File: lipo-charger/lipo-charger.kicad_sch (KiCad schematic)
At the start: 8 parts, among them J1 USB_B_Micro, U1 MCP73831-2-OT

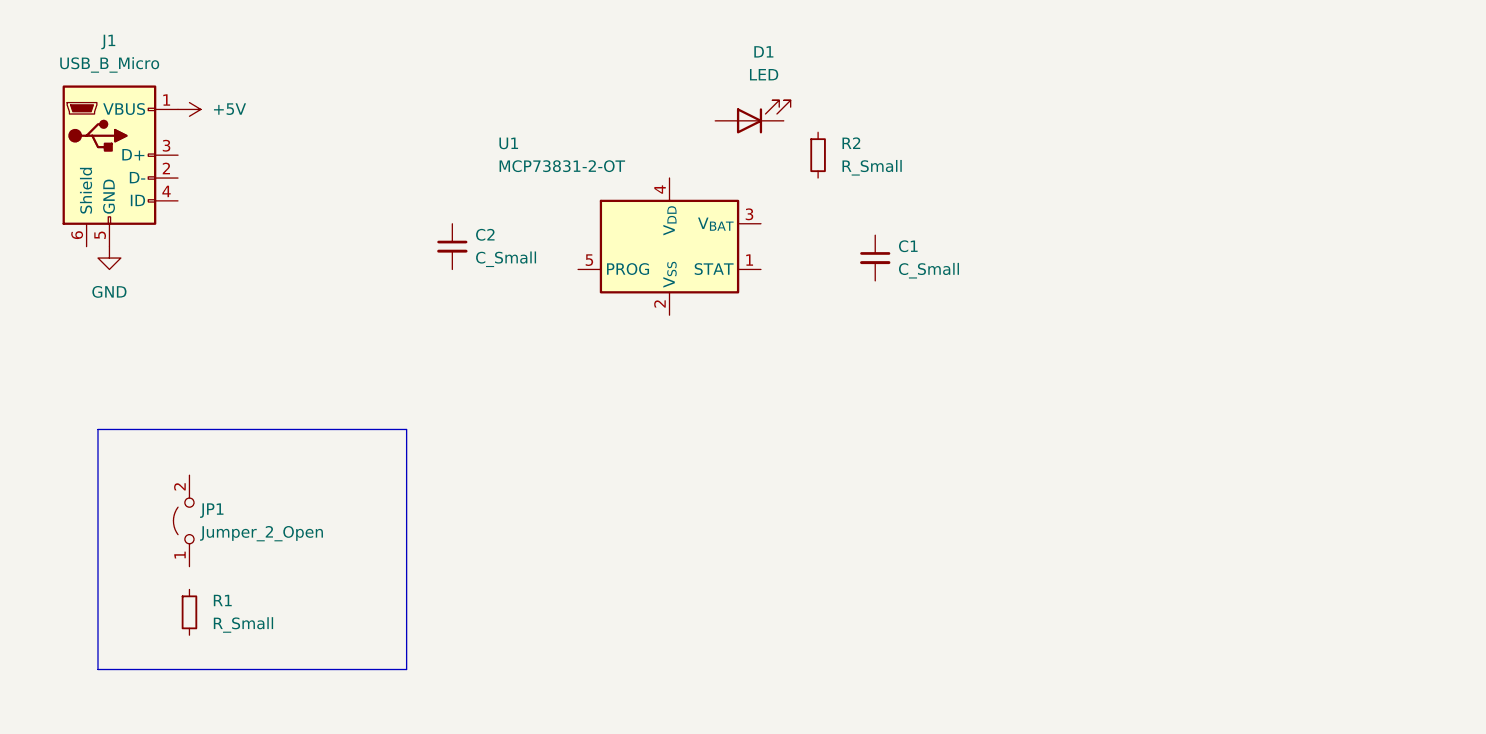
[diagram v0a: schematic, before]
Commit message: add prog resistor
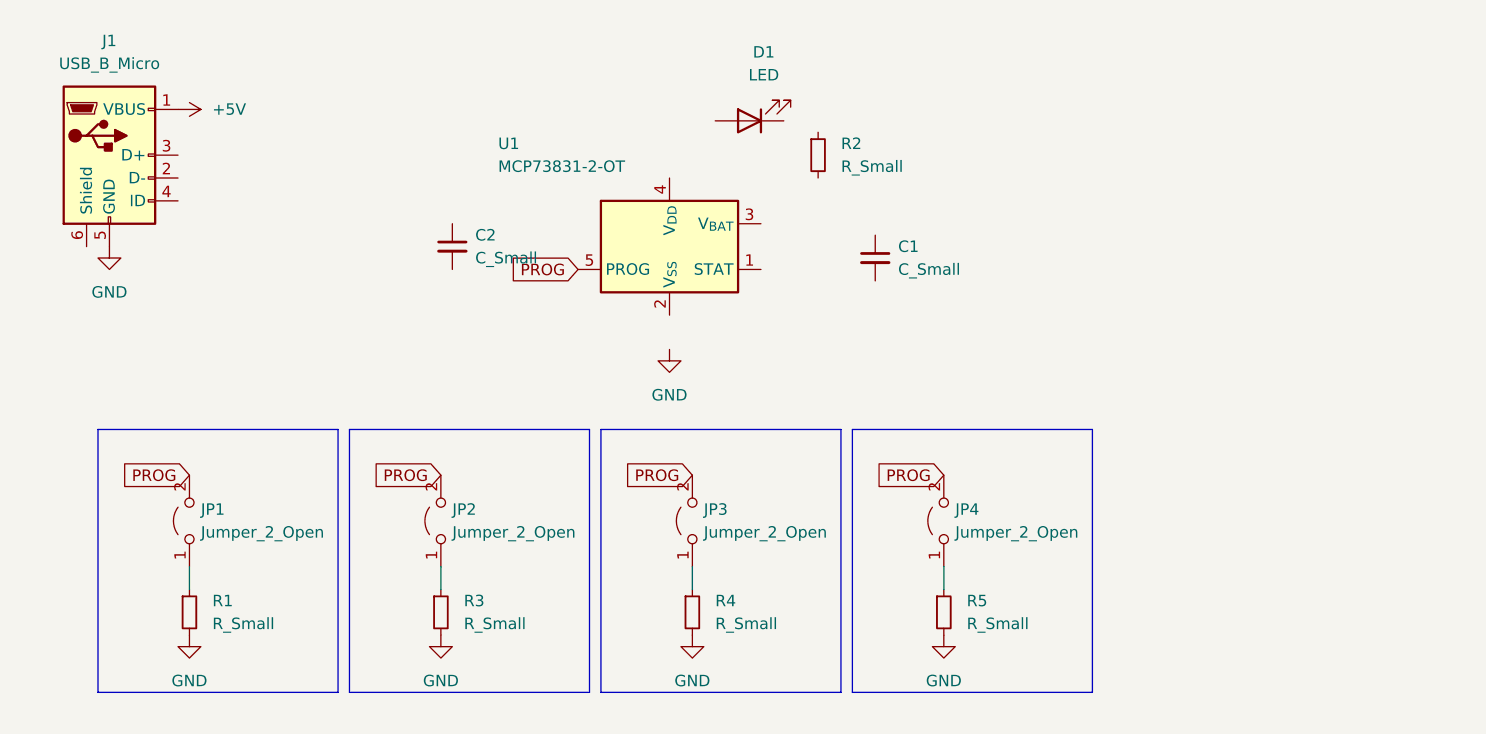
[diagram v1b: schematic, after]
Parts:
- added JP2, JP3, JP4: Jumper_2_Open, symbol Jumper:Jumper_2_Open
- added R3, R4, R5: R_Small, symbol Device:R_Small
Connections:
- net GND: now also R1.2, R3.2, R4.2, R5.2
- net at JP1.1 (A): now also R1.1
- net PROG: now reaches JP1.2 (B)
- net PROG: now also U1.5 (PROG), JP2.2 (B), JP3.2 (B), JP4.2 (B)
- new net: JP4.1 (A), R5.1
- new net: JP3.1 (A), R4.1
- new net: JP2.1 (A), R3.1

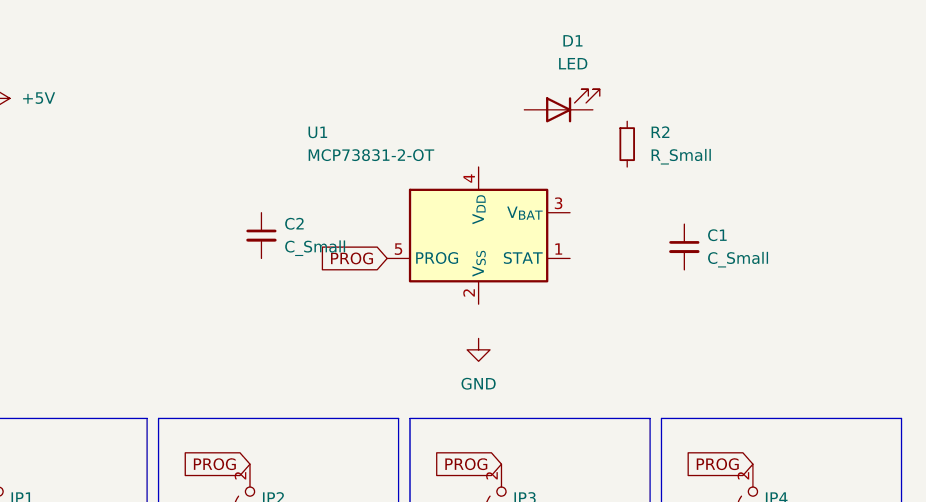
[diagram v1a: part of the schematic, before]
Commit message: mcp73 wired
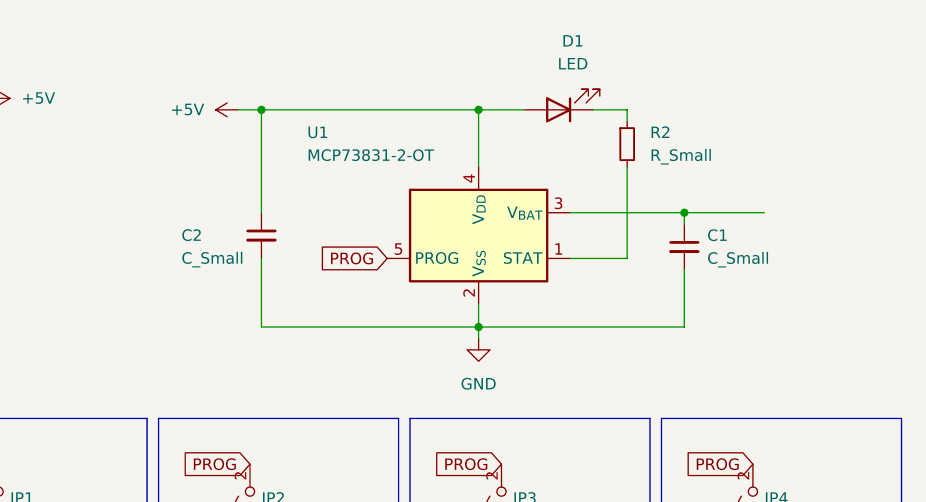
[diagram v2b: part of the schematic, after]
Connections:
- net +5V: now also C2.1, D1.2 (A), U1.4 (V_{DD})
- net GND: now also C1.2, C2.2, U1.2 (V_{SS})
- net at U1.1 (STAT): now also R2.2
- net at U1.3 (V_{BAT}): now also C1.1
- net at D1.1 (K): now also R2.1
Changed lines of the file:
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@@
 (kicad_sch (version 20230121) (generator eeschema)
   (paper "A4")
+  (junction (at 86.36 25.4) (diameter 0) (color 0 0 0 0)
+  )
+  (junction (at 86.36 49.53) (diameter 0) (color 0 0 0 0)
+  )
+  (junction (at 62.23 25.4) (diameter 0) (color 0 0 0 0)
+  )
+  (junction (at 109.22 36.83) (diameter 0) (color 0 0 0 0)
+  )
+  (wire (pts (xy 109.22 36.83) (xy 109.22 38.1))
+    (stroke (width 0) (type default))
+  )
   (polyline (pts (xy 50.8 59.69) (xy 77.47 59.69))
     (stroke (width 0) (type default))
@@
     (stroke (width 0) (type default))
   )
+  (wire (pts (xy 86.36 25.4) (xy 86.36 31.75))
+    (stroke (width 0) (type default))
+  )
+  (wire (pts (xy 109.22 36.83) (xy 118.11 36.83))
+    (stroke (width 0) (type default))
+  )
   (wire (pts (xy 60.96 74.93) (xy 60.96 77.47))
     (stroke (width 0) (type default))
@@
     (stroke (width 0) (type default))
   )
+  (wire (pts (xy 102.87 26.67) (xy 102.87 25.4))
+    (stroke (width 0) (type default))
+  )
+  (wire (pts (xy 96.52 41.91) (xy 102.87 41.91))
+    (stroke (width 0) (type default))
+  )
   (polyline (pts (xy 106.68 59.69) (xy 133.35 59.69))
     (stroke (width 0) (type default))
@@
     (stroke (width 0) (type default))
   )
+  (wire (pts (xy 102.87 41.91) (xy 102.87 31.75))
+    (stroke (width 0) (type default))
+  )
   (polyline (pts (xy 105.41 59.69) (xy 105.41 88.9))
     (stroke (width 0) (type default))
@@
     (stroke (width 0) (type default))
   )
+  (wire (pts (xy 86.36 25.4) (xy 62.23 25.4))
+    (stroke (width 0) (type default))
+  )
   (polyline (pts (xy 106.68 59.69) (xy 106.68 88.9))
     (stroke (width 0) (type default))
   )
+  (wire (pts (xy 86.36 46.99) (xy 86.36 49.53))
+    (stroke (width 0) (type default))
+  )
+  (wire (pts (xy 109.22 43.18) (xy 109.22 49.53))
+    (stroke (width 0) (type default))
+  )
+  (wire (pts (xy 91.44 25.4) (xy 86.36 25.4))
+    (stroke (width 0) (type default))
+  )
+  (wire (pts (xy 86.36 49.53) (xy 86.36 50.8))
+    (stroke (width 0) (type default))
+  )
+  (wire (pts (xy 62.23 25.4) (xy 62.23 36.83))
+    (stroke (width 0) (type default))
+  )
+  (wire (pts (xy 62.23 41.91) (xy 62.23 49.53))
+    (stroke (width 0) (type default))
+  )
+  (wire (pts (xy 62.23 49.53) (xy 86.36 49.53))
+    (stroke (width 0) (type default))
+  )
   (polyline (pts (xy 22.86 59.69) (xy 22.86 88.9))
     (stroke (width 0) (type default))
@@
     (stroke (width 0) (type default))
   )
+  (wire (pts (xy 102.87 25.4) (xy 99.06 25.4))
+    (stroke (width 0) (type default))
+  )
   (wire (pts (xy 33.02 74.93) (xy 33.02 77.47))
     (stroke (width 0) (type default))
   )
+  (wire (pts (xy 96.52 36.83) (xy 109.22 36.83))
+    (stroke (width 0) (type default))
+  )
   (polyline (pts (xy 78.74 59.69) (xy 78.74 88.9))
     (stroke (width 0) (type default))
   )
   (polyline (pts (xy 49.53 88.9) (xy 22.86 88.9))
+    (stroke (width 0) (type default))
+  )
+  (wire (pts (xy 59.69 25.4) (xy 62.23 25.4))
+    (stroke (width 0) (type default))
+  )
+  (wire (pts (xy 109.22 49.53) (xy 86.36 49.53))
     (stroke (width 0) (type default))
   )
@@
     )
   )
+  (symbol (lib_id "power:+5V") (at 59.69 25.4 90) (unit 1)
+    (in_bom yes) (on_board yes) (dnp no) (fields_autoplaced)
+    (property "Reference" "#PWR08" (at 63.5 25.4 0)
+      (effects (font (size 1.27 1.27)) hide)
+    )
+    (property "Value" "+5V" (at 55.88 25.4 90)
+      (effects (font (size 1.27 1.27)) (justify left))
+    )
+    (property "Footprint" "" (at 59.69 25.4 0)
+      (effects (font (size 1.27 1.27)) hide)
+    )
+    (property "Datasheet" "" (at 59.69 25.4 0)
+      (effects (font (size 1.27 1.27)) hide)
+    )
+    (pin "1")
+    (instances
+      (project "lipo-charger"
+        (path "/6ab53b90-6b93-43c8-ba73-afd37b7c177a"
+          (reference "#PWR08") (unit 1)
+        )
+      )
+    )
+  )
   (symbol (lib_id "Device:R_Small") (at 60.96 80.01 0) (unit 1)
     (in_bom yes) (on_board yes) (dnp no) (fields_autoplaced)
@@
   )
   (symbol (lib_id "Device:C_Small") (at 62.23 39.37 0) (unit 1)
-    (in_bom yes) (on_board yes) (dnp no) (fields_autoplaced)
-    (property "Reference" "C2" (at 64.77 38.1063 0)
-      (effects (font (size 1.27 1.27)) (justify left))
-    )
-    (property "Value" "C_Small" (at 64.77 40.6463 0)
-      (effects (font (size 1.27 1.27)) (justify left))
-    )
+    (in_bom yes) (on_board yes) (dnp no)
+    (property "Reference" "C2" (at 53.34 39.37 0)
+      (effects (font (size 1.27 1.27)) (justify left))
+    )
+    (property "Value" "C_Small" (at 53.34 41.91 0)
+      (effects (font (size 1.27 1.27)) (justify left))
+    )

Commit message: first pcb placed
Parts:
- C1, C2: footprint (none) -> Capacitor_SMD:C_0603_1608Metric
- D1: footprint (none) -> LED_SMD:LED_0603_1608Metric
- J1: footprint (none) -> Connector_USB:USB_Micro-B_Molex-105017-0001
- JP1, JP2, JP3, JP4: footprint (none) -> Jumper:SolderJumper-2_P1.3mm_Open_TrianglePad1.0x1.5mm
- R1, R2, R3, R4, R5: footprint (none) -> Resistor_SMD:R_0603_1608Metric
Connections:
- net LIPO: now reaches C1.1, U1.3 (V_{BAT})
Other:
- moved on the sheet: JP1, JP2, JP3, JP4, R1, R3, R4, R5

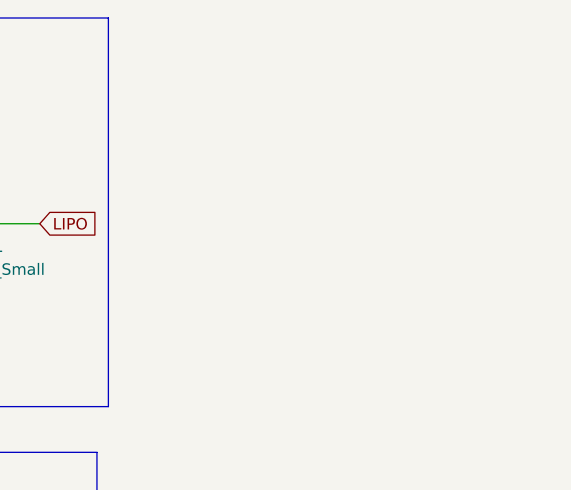
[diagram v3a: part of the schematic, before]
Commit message: add connector
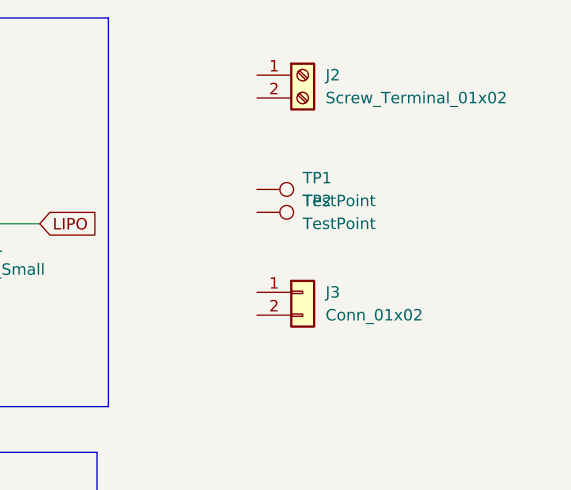
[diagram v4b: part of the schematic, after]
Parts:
- added J2: Screw_Terminal_01x02, Connector_Molex:Molex_KK-254_AE-6410-02A_1x02_P2.54mm_Vertical, symbol Connector:Screw_Terminal_01x02
- added J3: Conn_01x02, Connector_JST:JST_PH_B2B-PH-K_1x02_P2.00mm_Vertical, symbol Connector_Generic:Conn_01x02
- added TP1, TP2: TestPoint, Connector_Pin:Pin_D0.7mm_L6.5mm_W1.8mm_FlatFork, symbol Connector:TestPoint
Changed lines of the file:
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@@
+    )
+  )
+  (symbol (lib_id "Connector_Generic:Conn_01x02") (at 147.32 44.45 0) (unit 1)
+    (in_bom yes) (on_board yes) (dnp no) (fields_autoplaced)
+    (property "Reference" "J3" (at 149.86 44.45 0)
+      (effects (font (size 1.27 1.27)) (justify left))
+    )
+    (property "Value" "Conn_01x02" (at 149.86 46.99 0)
+      (effects (font (size 1.27 1.27)) (justify left))
+    )
+    (property "Footprint" "Connector_JST:JST_PH_B2B-PH-K_1x02_P2.00mm_Vertical" (at 147.32 44.45 0)
+      (effects (font (size 1.27 1.27)) hide)
+    )
+    (property "Datasheet" "~" (at 147.32 44.45 0)
+      (effects (font (size 1.27 1.27)) hide)
+    )
+    (pin "1")
+    (pin "2")
+    (instances
+      (project "lipo-charger"
+        (path "/6ab53b90-6b93-43c8-ba73-afd37b7c177a"
+          (reference "J3") (unit 1)
+        )
+      )
     )
   )
@@
         (path "/6ab53b90-6b93-43c8-ba73-afd37b7c177a"
           (reference "#PWR01") (unit 1)
+        )
+      )
+    )
+  )
+  (symbol (lib_id "Connector:Screw_Terminal_01x02") (at 147.32 20.32 0) (unit 1)
+    (in_bom yes) (on_board yes) (dnp no) (fields_autoplaced)
+    (property "Reference" "J2" (at 149.86 20.32 0)
+      (effects (font (size 1.27 1.27)) (justify left))
+    )
+    (property "Value" "Screw_Terminal_01x02" (at 149.86 22.86 0)
+      (effects (font (size 1.27 1.27)) (justify left))
+    )
+    (property "Footprint" "Connector_Molex:Molex_KK-254_AE-6410-02A_1x02_P2.54mm_Vertical" (at 147.32 20.32 0)
+      (effects (font (size 1.27 1.27)) hide)
+    )
+    (property "Datasheet" "~" (at 147.32 20.32 0)
+      (effects (font (size 1.27 1.27)) hide)
+    )
+    (pin "1")
+    (pin "2")
+    (instances
+      (project "lipo-charger"
+        (path "/6ab53b90-6b93-43c8-ba73-afd37b7c177a"
+          (reference "J2") (unit 1)
         )
       )
@@
     )
   )
+  (symbol (lib_id "Connector:TestPoint") (at 142.24 33.02 270) (unit 1)
+    (in_bom yes) (on_board yes) (dnp no) (fields_autoplaced)
+    (property "Reference" "TP1" (at 147.32 31.75 90)
+      (effects (font (size 1.27 1.27)) (justify left))
+    )
+    (property "Value" "TestPoint" (at 147.32 34.29 90)
+      (effects (font (size 1.27 1.27)) (justify left))
+    )
+    (property "Footprint" "Connector_Pin:Pin_D0.7mm_L6.5mm_W1.8mm_FlatFork" (at 142.24 38.1 0)
+      (effects (font (size 1.27 1.27)) hide)
+    )
+    (property "Datasheet" "~" (at 142.24 38.1 0)
+      (effects (font (size 1.27 1.27)) hide)
+    )
+    (pin "1")
+    (instances
+      (project "lipo-charger"
+        (path "/6ab53b90-6b93-43c8-ba73-afd37b7c177a"
+          (reference "TP1") (unit 1)
+        )
+      )
+    )
+  )
   (symbol (lib_id "Device:C_Small") (at 62.23 39.37 0) (unit 1)
     (in_bom yes) (on_board yes) (dnp no)
@@
         )
       )
+    )
+  )
+  (symbol (lib_id "Connector:TestPoint") (at 142.24 35.56 270) (unit 1)
+    (in_bom yes) (on_board yes) (dnp no) (fields_autoplaced)
+    (property "Reference" "TP2" (at 147.32 34.29 90)
+      (effects (font (size 1.27 1.27)) (justify left))
+    )
+    (property "Value" "TestPoint" (at 147.32 36.83 90)
+      (effects (font (size 1.27 1.27)) (justify left))
+    )
+    (property "Footprint" "Connector_Pin:Pin_D0.7mm_L6.5mm_W1.8mm_FlatFork" (at 142.24 40.64 0)
+      (effects (font (size 1.27 1.27)) hide)
+    )
+    (property "Datasheet" "~" (at 142.24 40.64 0)
+      (effects (font (size 1.27 1.27)) hide)
+    )
+    (pin "1")
+    (instances
+      (project "lipo-charger"
+        (path "/6ab53b90-6b93-43c8-ba73-afd37b7c177a"
+          (reference "TP2") (unit 1)
+        )
+      )

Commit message: update test + final wiring
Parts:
- R1: value R_Small -> 20k
- R3: value R_Small -> 10k
- R4: value R_Small -> 5k
- R5: value R_Small -> 2k
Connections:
- net GND: now also J2.2 (Pin_2), J3.2 (Pin_2), TP2.1
- net LIPO: now also J2.1 (Pin_1), J3.1 (Pin_1), TP1.1
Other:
- note added: "100ma"
- note added: "200ma"
- note added: "500ma"
- note added: "50ma"
- note added: "USB CONNECTOR"
- moved on the sheet: J1
